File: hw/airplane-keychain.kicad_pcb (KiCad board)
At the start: 2 copper layers, 12 parts, among them IC1 ATTINY85-P, SW1 SW_PUSH, SW2 SPST

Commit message: Tests with board outline
Not going so well :(
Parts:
- removed G*: LOGO, lib:airplane_lrg
- added G***: LOGO, lib:huge_aircraft, F.Cu at (135.9, 92.7)
- moved D2 19.0 mm to (85.1, 92.7)
- moved D1 17.8 mm to (90.2, 92.7)
- moved D3 16.7 mm to (161.3, 152.4)
- moved D5 16.5 mm to (153.7, 152.4)
- moved D4 15.5 mm to (161.3, 33.0)
- moved D6 15.2 mm to (153.7, 33.0)
- moved D7 10.2 mm to (184.2, 96.5)

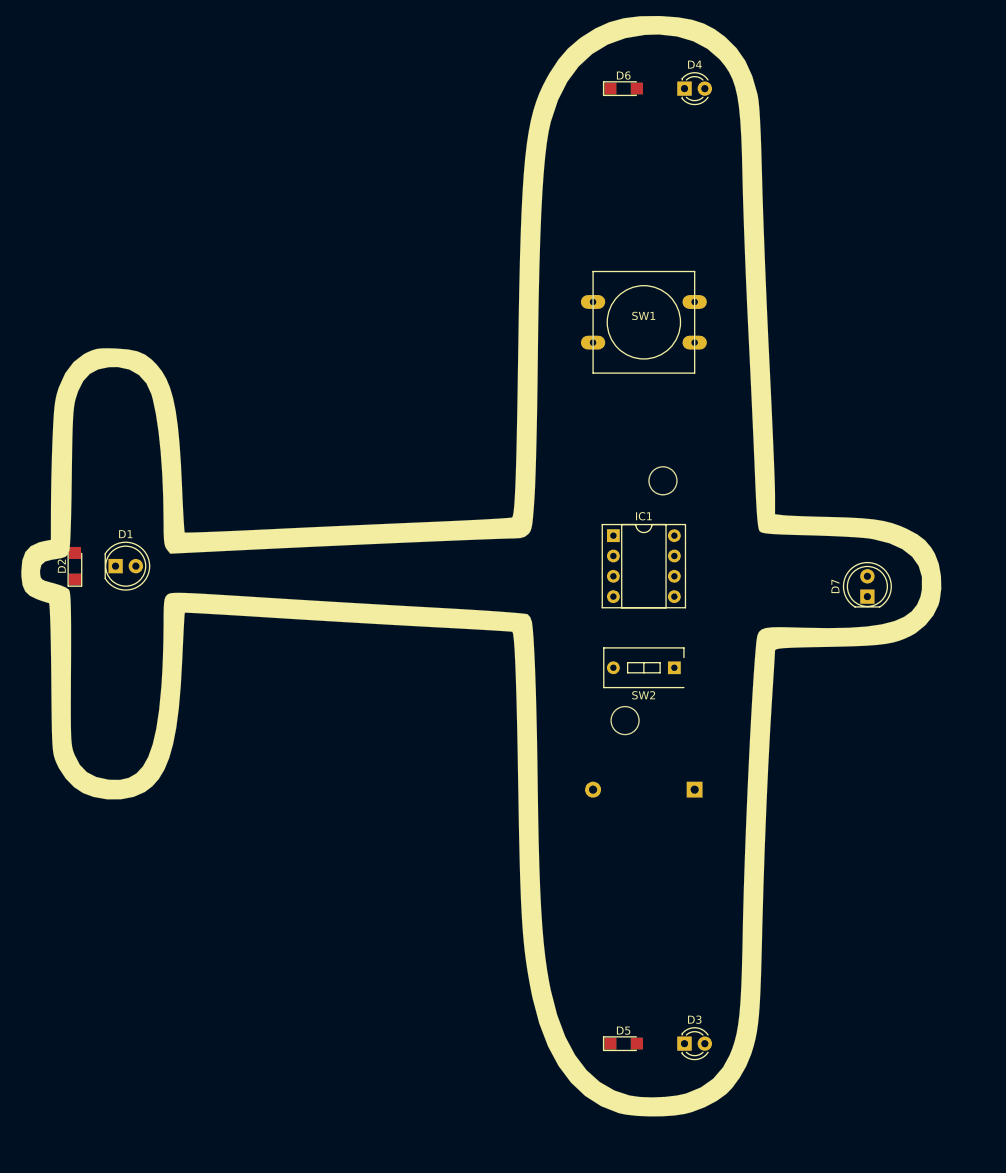
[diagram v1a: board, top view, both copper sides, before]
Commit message: added current limiting resistors
swapped out battery connector
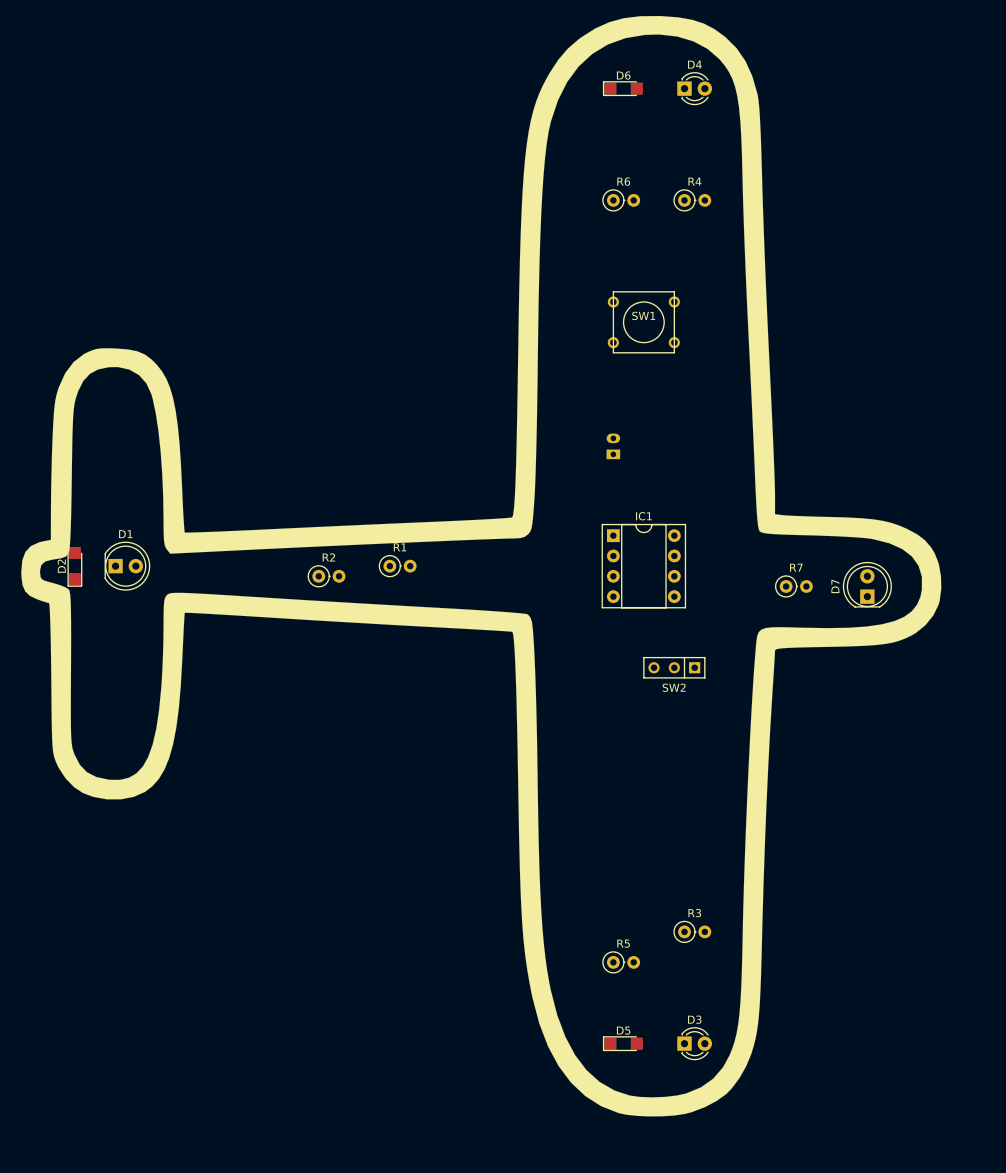
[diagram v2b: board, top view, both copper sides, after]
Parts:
- added R1: 100, Resistors_ThroughHole:R_Axial_DIN0207_L6.3mm_D2.5mm_P2.54mm_Vertical, F.Cu at (124.5, 92.7)
- added R2: 100, Resistors_ThroughHole:R_Axial_DIN0207_L6.3mm_D2.5mm_P2.54mm_Vertical, F.Cu at (115.6, 94.0)
- added R3: 100, Resistors_ThroughHole:R_Axial_DIN0207_L6.3mm_D2.5mm_P2.54mm_Vertical, F.Cu at (161.3, 138.4)
- added R4: 100, Resistors_ThroughHole:R_Axial_DIN0207_L6.3mm_D2.5mm_P2.54mm_Vertical, F.Cu at (161.3, 47.0)
- added R5: 100, Resistors_ThroughHole:R_Axial_DIN0207_L6.3mm_D2.5mm_P2.54mm_Vertical, F.Cu at (152.4, 142.2)
- added R6: 100, Resistors_ThroughHole:R_Axial_DIN0207_L6.3mm_D2.5mm_P2.54mm_Vertical, F.Cu at (152.4, 47.0)
- added R7: 50, Resistors_ThroughHole:R_Axial_DIN0207_L6.3mm_D2.5mm_P2.54mm_Vertical, F.Cu at (174.0, 95.2)
- BT1: footprint Battery_Holders:Keystone_2468_2xAAA -> Connectors_JST:JST_PH_B2B-PH-K_02x2.00mm_Straight
- SW1: footprint Buttons_Switches_ThroughHole:SW_PUSH-12mm -> Buttons_Switches_ThroughHole:SW_PUSH_SMALL
- SW2: footprint Buttons_Switches_ThroughHole:SW_DIP_x1_W7.62mm_Slide -> Buttons_Switches_ThroughHole:SW_Micro_SPST
- moved BT1 43.1 mm to (152.4, 78.7)
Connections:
- IC1 pad 1: Net-(D6-Pad2) -> Net-(IC1-Pad1)
- IC1 pad 2: Net-(D4-Pad2) -> Net-(IC1-Pad2)
- IC1 pad 3: Net-(D5-Pad2) -> Net-(IC1-Pad3)
- IC1 pad 5: Net-(D1-Pad2) -> Net-(IC1-Pad5)
- IC1 pad 6: Net-(D2-Pad2) -> Net-(IC1-Pad6)
- IC1 pad 7: Net-(D3-Pad2) -> Net-(IC1-Pad7)
- SW1 pad 1: Net-(D7-Pad2) -> Net-(R7-Pad1)

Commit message: Added second battery
Changed some footprints
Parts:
- removed G***: LOGO, lib:huge_aircraft
- added BT2: Battery_Cell, Battery_Holders:Keystone_1058_1x2032-CoinCell, F.Cu at (157.5, 121.9)
- BT1: value Battery -> Battery_Cell; footprint Connectors_JST:JST_PH_B2B-PH-K_02x2.00mm_Straight -> Battery_Holders:Keystone_1058_1x2032-CoinCell
- R1, R2, R3, R4, R5, R6, R7: footprint Resistors_ThroughHole:R_Axial_DIN0207_L6.3mm_D2.5mm_P2.54mm_Vertical -> Resistors_ThroughHole:R_Axial_DIN0411_L9.9mm_D3.6mm_P5.08mm_Vertical
- SW1: footprint Buttons_Switches_ThroughHole:SW_PUSH_SMALL -> Buttons_Switches_ThroughHole:SW_PUSH_6mm_h9.5mm

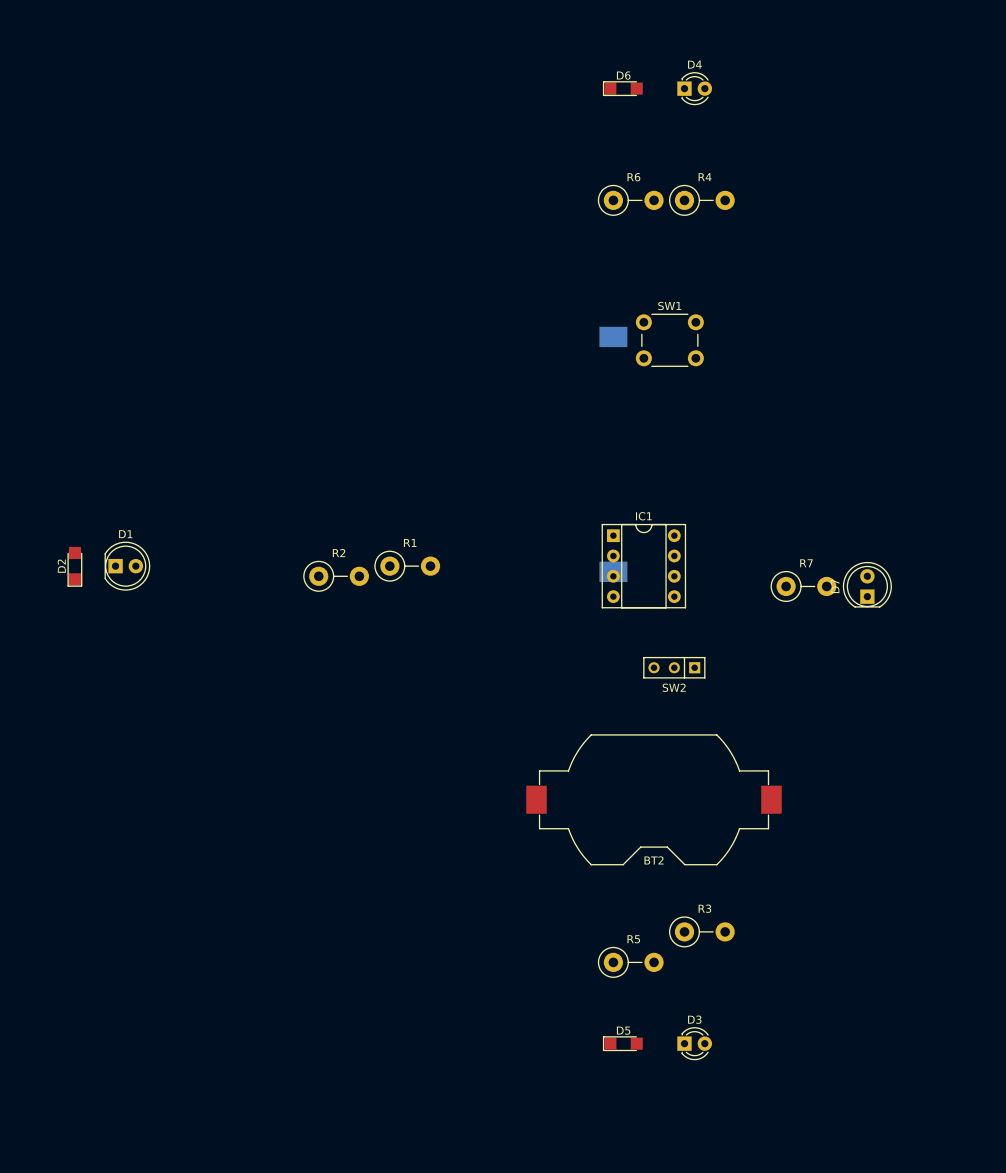
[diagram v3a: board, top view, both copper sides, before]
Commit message: Added aircraft outline
Changed board edges to aircraft outline
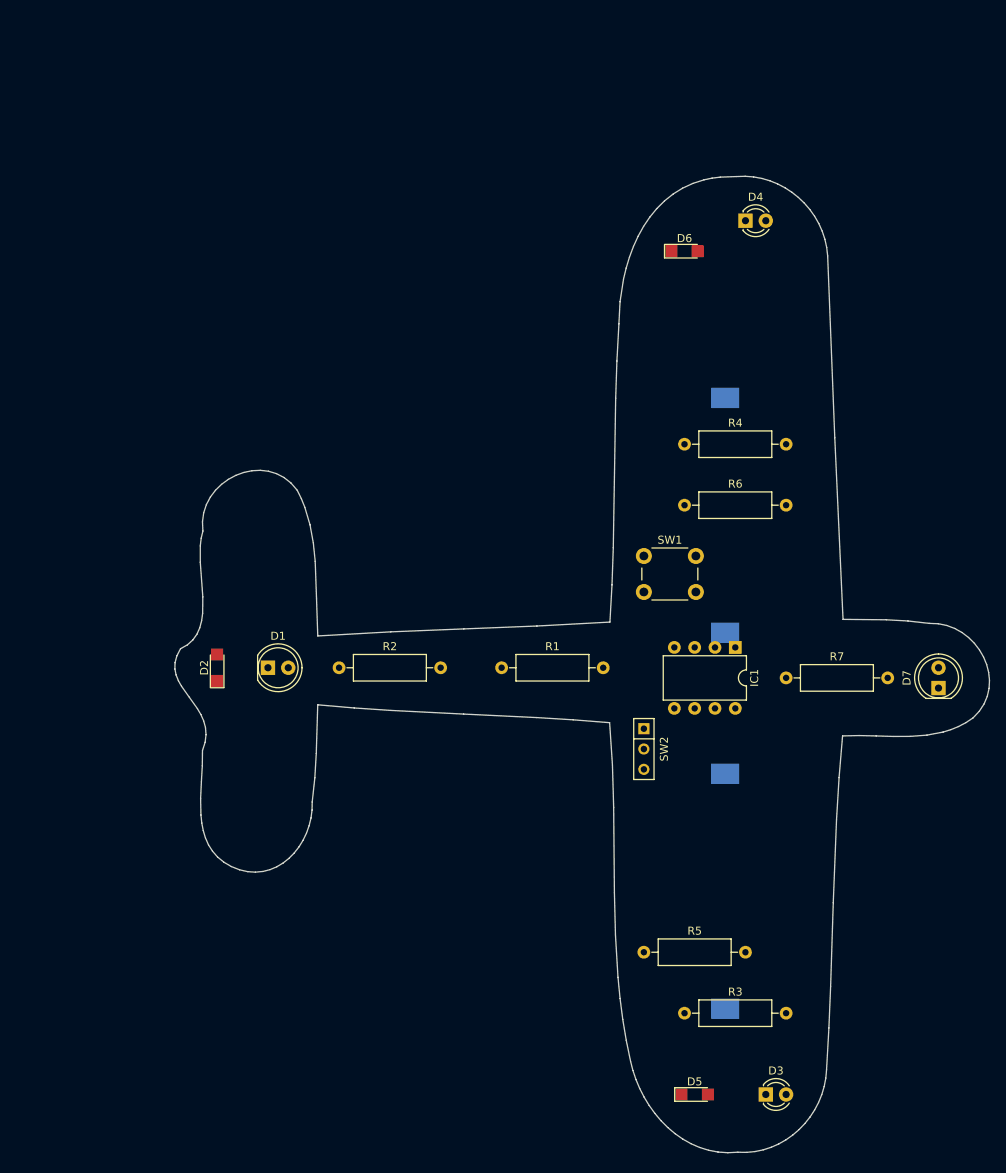
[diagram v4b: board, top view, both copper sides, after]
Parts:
- BT2: moved to B.Cu
- IC1: footprint Housings_DIP:DIP-8_W7.62mm_Socket -> Housings_DIP:DIP-8_W7.62mm
- R1, R2, R3, R4, R5, R6, R7: footprint Resistors_ThroughHole:R_Axial_DIN0411_L9.9mm_D3.6mm_P5.08mm_Vertical -> Resistors_THT:R_Axial_DIN0309_L9.0mm_D3.2mm_P12.70mm_Horizontal
- SW1: footprint Buttons_Switches_ThroughHole:SW_PUSH_6mm_h9.5mm -> Buttons_Switches_THT:SW_PUSH_6mm
- SW2: footprint Buttons_Switches_ThroughHole:SW_Micro_SPST -> Buttons_Switches_THT:SW_Micro_SPST
- moved R6 39.1 mm to (161.3, 85.1)
- moved R4 30.5 mm to (161.3, 77.5)
- moved SW1 29.2 mm to (156.2, 91.4)
- moved D1 22.9 mm to (109.2, 105.4)
- moved D2 21.8 mm to (102.9, 105.4)
- moved D6 21.7 mm to (161.3, 53.3)
- moved IC1 20.7 mm to (167.6, 102.9), turned to 270 degrees
- moved R1 18.9 mm to (138.4, 105.4)
- moved D4 18.2 mm to (168.9, 49.5)
- moved BT1 15.9 mm to (166.4, 86.4)
- moved BT2 14.5 mm to (166.4, 133.3), turned to 270 degrees
- moved D7 14.5 mm to (193.0, 108.0)
- moved D3 12.0 mm to (171.4, 158.8)
- moved R2 11.7 mm to (118.1, 105.4)
- moved R7 11.4 mm to (174.0, 106.7)
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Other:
- board outline added: 101.8 x 122.1 mm

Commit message: First run routed board
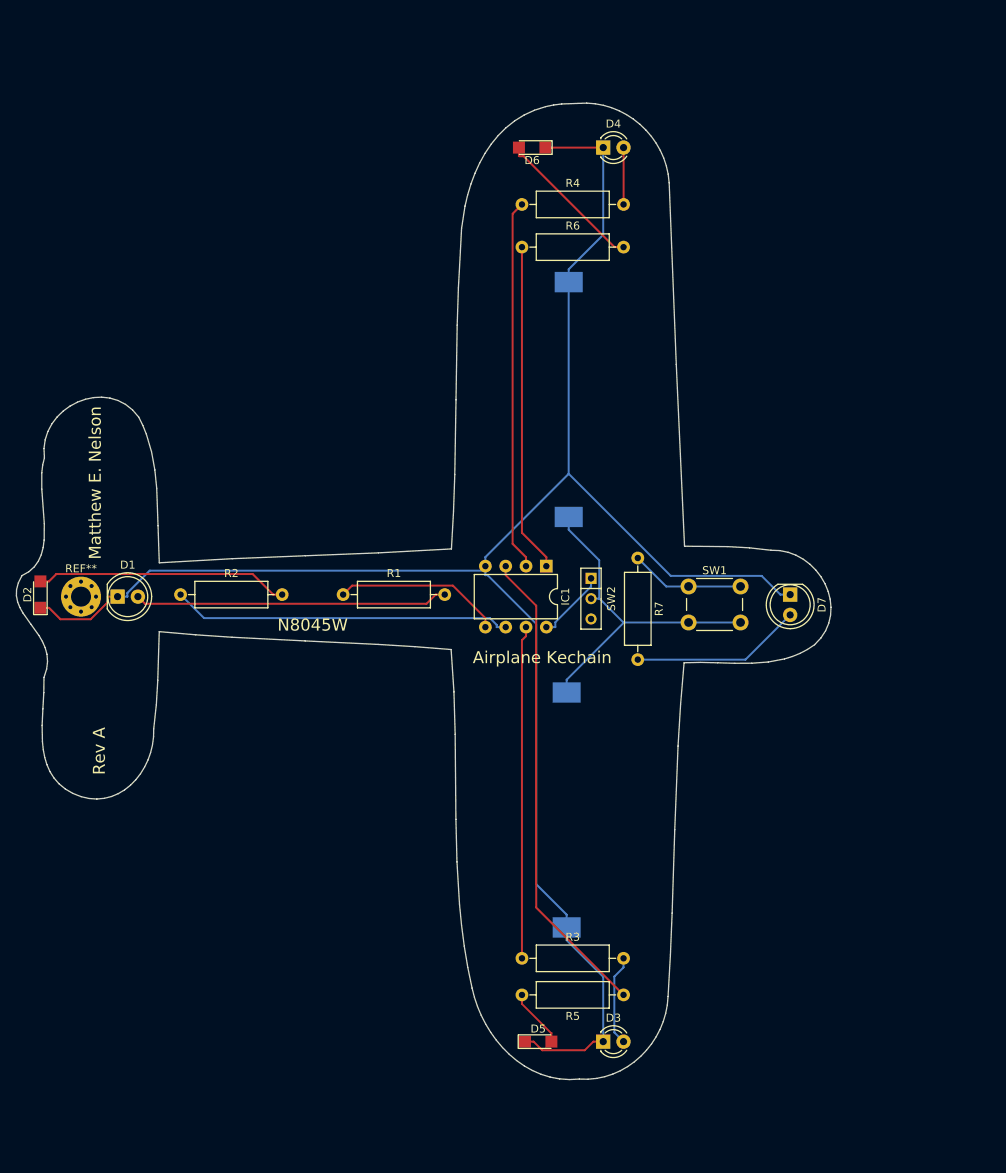
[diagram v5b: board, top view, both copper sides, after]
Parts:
- added REF**: MountingHole_2.5mm_Pad_Via, Mounting_Holes:MountingHole_2.5mm_Pad_Via, F.Cu at (85.9, 96.5)
- moved R6 38.1 mm to (141.0, 52.8)
- moved R4 36.2 mm to (141.0, 47.5)
- moved IC1 25.7 mm to (144.0, 92.7)
- moved BT1 24.3 mm to (146.8, 71.9)
- moved D2 23.9 mm to (80.8, 96.3)
- moved R7 23.8 mm to (155.4, 91.7), turned to 270 degrees
- moved D6 23.0 mm to (142.2, 40.4), turned to 180 degrees
- moved BT2 22.3 mm to (146.6, 123.2)
- moved D7 21.9 mm to (174.5, 96.3), turned to 270 degrees
- moved R1 21.8 mm to (118.6, 96.3)
- moved R2 21.8 mm to (98.3, 96.3)
- moved R3 21.4 mm to (141.0, 141.7)
- moved D3 21.4 mm to (151.1, 152.1)
- moved D1 20.8 mm to (90.4, 96.5)
- moved D5 20.6 mm to (143.0, 152.1)
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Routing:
- net GND: track 0.00 -> 235.4 mm
- net Net-(IC1-Pad3): track 0.00 -> 59.7 mm
- net Net-(IC1-Pad2): track 0.00 -> 46.4 mm
- net Net-(BT1-Pad1): track 0.00 -> 43.4 mm
- net Net-(IC1-Pad6): track 0.00 -> 42.5 mm
- net Net-(IC1-Pad7): track 0.00 -> 41.6 mm
- net Net-(IC1-Pad1): track 0.00 -> 41.1 mm
- net Net-(D1-Pad2): track 0.00 -> 39.2 mm
- net Net-(D2-Pad2): track 0.00 -> 31.7 mm
- net Net-(D7-Pad2): track 0.00 -> 21.4 mm
- net Net-(IC1-Pad5): track 0.00 -> 21.1 mm
- net Net-(D6-Pad2): track 0.00 -> 18.9 mm
- net Net-(R7-Pad1): track 0.00 -> 14.3 mm
- net Net-(D3-Pad2): track 0.00 -> 11.4 mm
- net Net-(IC1-Pad8): track 0.00 -> 9.07 mm
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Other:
- board text added: "Airplane Kechain"
- board text added: "Matthew E. Nelson"
- board text added: "N8045W"
- board text added: "Rev A"

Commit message: Second trace run
Second attempt to routing and layout
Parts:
- removed REF**: MountingHole_2.5mm_Pad_Via, Mounting_Holes:MountingHole_2.5mm_Pad_Via
- added CHAIN1: MountingHole_2.7mm, Mounting_Holes:MountingHole_2.7mm, F.Cu at (85.3, 108.7)
- added CHAIN2: MountingHole_2.7mm, Mounting_Holes:MountingHole_2.7mm, F.Cu at (84.3, 83.1)
- moved R2 14.2 mm to (112.5, 96.3), turned to 180 degrees
- moved R6 12.5 mm to (153.4, 53.3), turned to 180 degrees
- moved R1 11.4 mm to (130.0, 96.3), turned to 180 degrees
- moved D1 1.37 mm to (90.9, 97.8), turned to 90 degrees
- moved SW2 0.80 mm to (149.9, 97.5), turned to 90 degrees
- moved R3 0.76 mm to (141.0, 141.0)
- moved R4 0.76 mm to (141.0, 46.7)
- moved D2 0.25 mm to (80.8, 96.5)
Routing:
- net Net-(IC1-Pad6): track 42.5 -> 28.3 mm
- net Net-(IC1-Pad5): track 21.1 -> 8.03 mm
- net Net-(D1-Pad2): track 39.2 -> 26.9 mm
- net Net-(D2-Pad2): track 31.7 -> 19.8 mm
- net Net-(D6-Pad2): track 18.9 -> 13.6 mm
- net Net-(IC1-Pad8): track 9.07 -> 5.95 mm
- net Net-(IC1-Pad1): track 41.1 -> 43.3 mm
- net Net-(IC1-Pad7): track 41.6 -> 40.9 mm
- net Net-(D4-Pad2): track 7.11 -> 6.35 mm
- net Net-(D3-Pad2): track 11.4 -> 12.1 mm
- net Net-(BT1-Pad1): track 43.4 -> 42.8 mm
